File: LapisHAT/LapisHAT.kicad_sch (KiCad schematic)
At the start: 0 parts

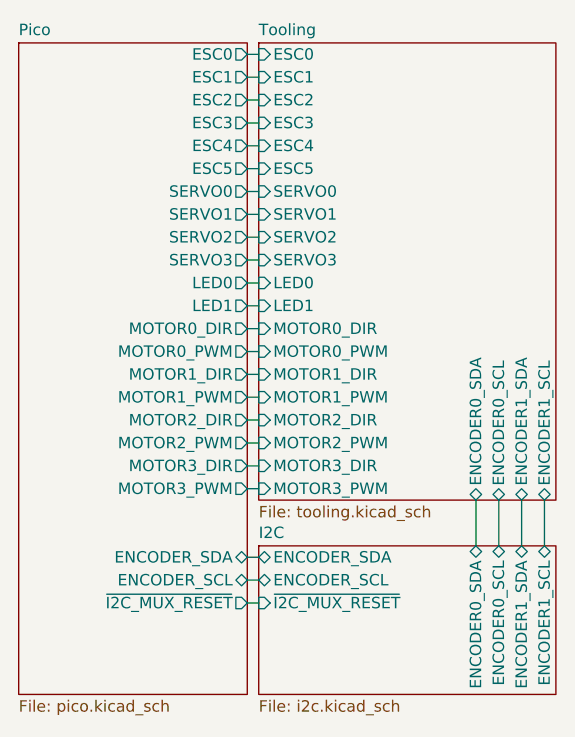
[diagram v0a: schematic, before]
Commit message: New Lapis Hat
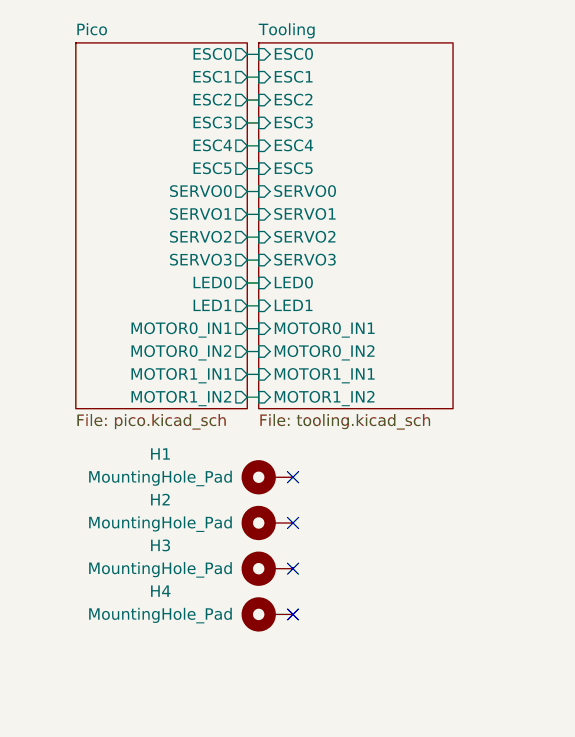
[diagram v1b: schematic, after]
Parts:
- added H1, H2, H3, H4: MountingHole_Pad, MountingHole:MountingHole_2.7mm_M2.5_Pad_Via, symbol Mechanical:MountingHole_Pad
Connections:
- no-connect marks 0 -> 4
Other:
- removed sheet I2C
- sheet Pico ports: added MOTOR0_IN1, MOTOR0_IN2, MOTOR1_IN1, MOTOR1_IN2; removed ENCODER_SCL, ENCODER_SDA, MOTOR0_DIR, MOTOR0_PWM, MOTOR1_DIR, MOTOR1_PWM, MOTOR2_DIR, MOTOR2_PWM, MOTOR3_DIR, MOTOR3_PWM, ~{I2C_MUX_RESET}
- sheet Tooling ports: added MOTOR0_IN1, MOTOR0_IN2, MOTOR1_IN1, MOTOR1_IN2; removed ENCODER0_SCL, ENCODER0_SDA, ENCODER1_SCL, ENCODER1_SDA, MOTOR0_DIR, MOTOR0_PWM, MOTOR1_DIR, MOTOR1_PWM, MOTOR2_DIR, MOTOR2_PWM, MOTOR3_DIR, MOTOR3_PWM

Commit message: Some review changes
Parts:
- H1, H2, H3, H4: footprint MountingHole:MountingHole_2.7mm_M2.5_Pad_Via -> MountingHole:MountingHole_3.2mm_M3_Pad_Via
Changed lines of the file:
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@@
 			)
 		)
-		(property "Footprint" "MountingHole:MountingHole_2.7mm_M2.5_Pad_Via"
+		(property "Footprint" "MountingHole:MountingHole_3.2mm_M3_Pad_Via"
 			(at 44.45 67.31 0)
 			(effects
@@
 			)
 		)
-		(property "Footprint" "MountingHole:MountingHole_2.7mm_M2.5_Pad_Via"
+		(property "Footprint" "MountingHole:MountingHole_3.2mm_M3_Pad_Via"
 			(at 44.45 82.55 0)
 			(effects
@@
 			)
 		)
-		(property "Footprint" "MountingHole:MountingHole_2.7mm_M2.5_Pad_Via"
+		(property "Footprint" "MountingHole:MountingHole_3.2mm_M3_Pad_Via"
 			(at 44.45 72.39 0)
 			(effects
@@
 			)
 		)
-		(property "Footprint" "MountingHole:MountingHole_2.7mm_M2.5_Pad_Via"
+		(property "Footprint" "MountingHole:MountingHole_3.2mm_M3_Pad_Via"
 			(at 44.45 77.47 0)
 			(effects
